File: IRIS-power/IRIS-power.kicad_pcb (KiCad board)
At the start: 2 copper layers, 65 x 65 mm, 84 parts, among them J11 Powerpole, J12 PJ-047AH, J13 Conn_01x20_MountingPin, Q21 2N7002, Q61 DMP2066LSN-7, U21 MAX17261, U31 TPS2121, U41 TPS55340, U51 TPSM53604, U61 LTC3110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

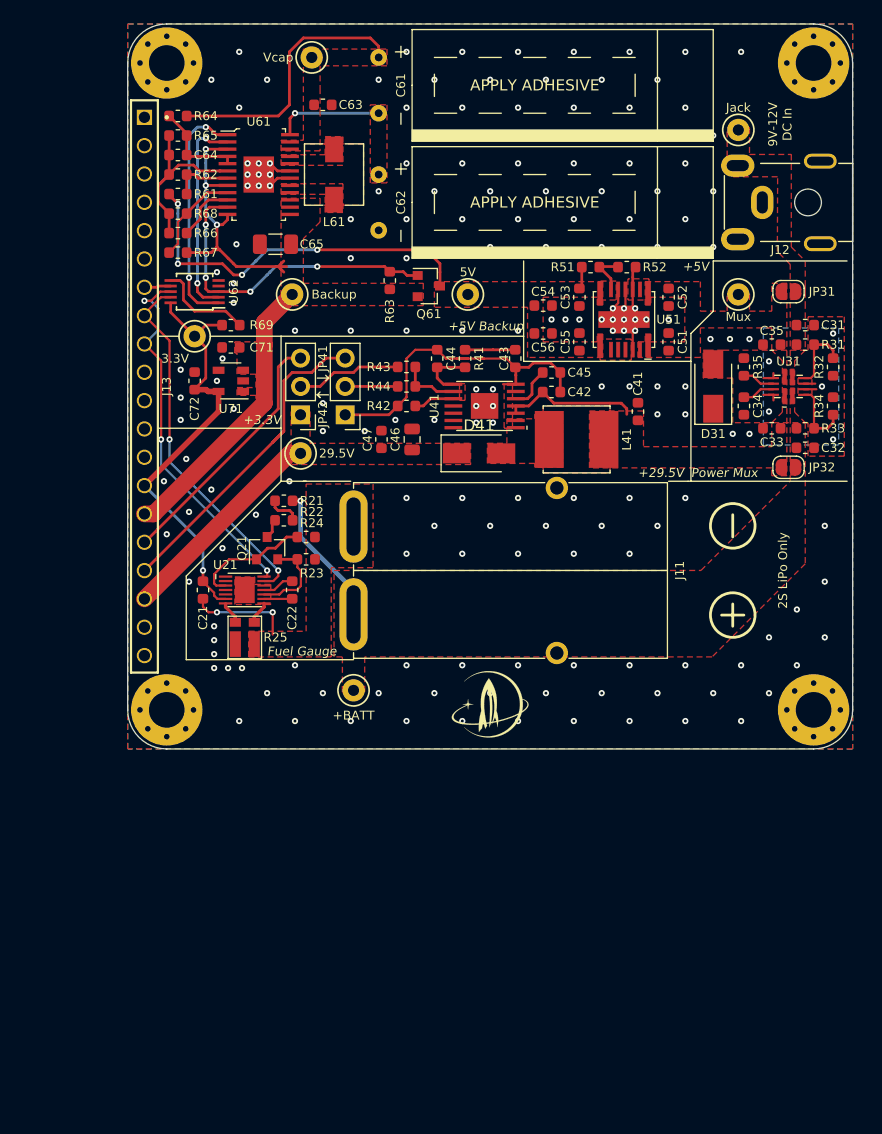
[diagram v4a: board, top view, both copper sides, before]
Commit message: USB C power prototype
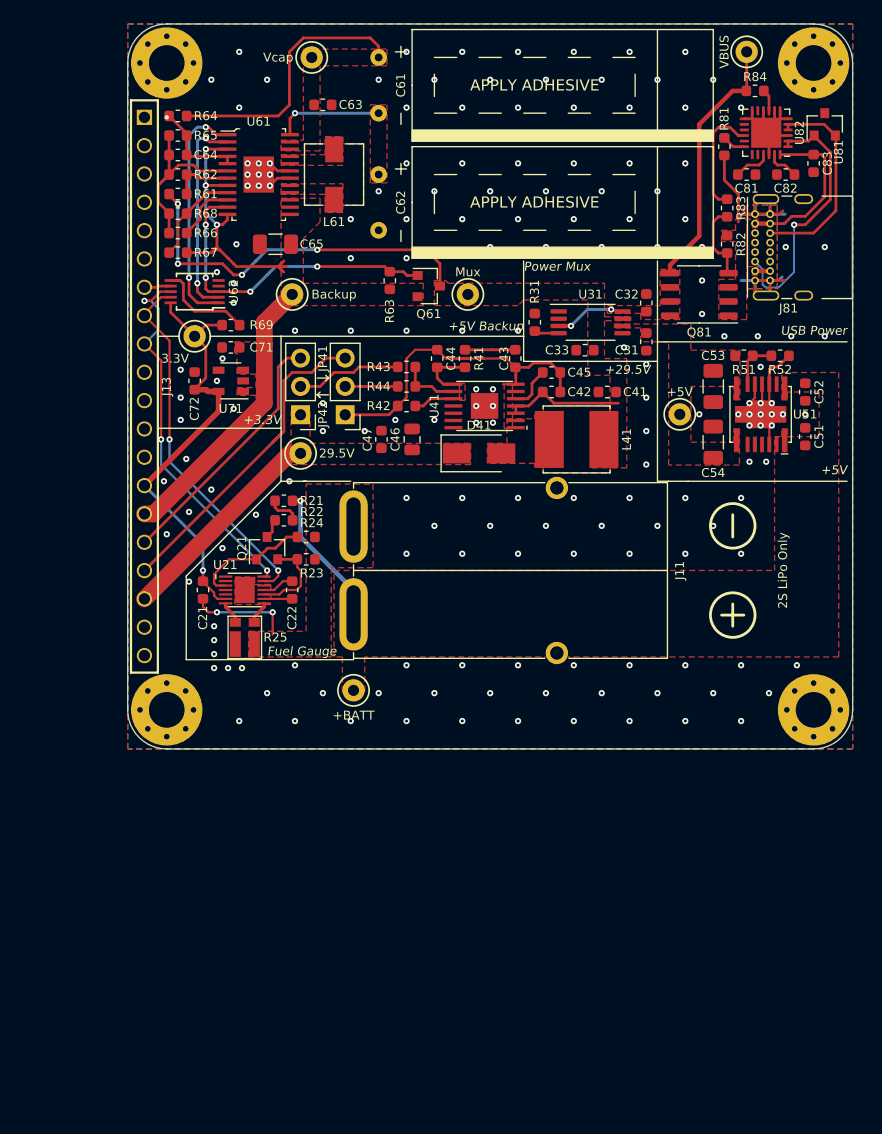
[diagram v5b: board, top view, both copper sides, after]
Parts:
- removed C34: 1uF, Capacitor_SMD:C_0603_1608Metric
- removed C35, C55, C56: 10uF, Capacitor_SMD:C_0603_1608Metric
- removed D31: D_Schottky, Diode_SMD:D_SMA
- removed G***: LOGO, star-common-lib:star_7x6
- removed J12: PJ-047AH, star-common-lib:CUI_PJ-047AH
- removed JP31: DC Jack Bypass, Jumper:SolderJumper-2_P1.3mm_Open_RoundedPad1.0x1.5mm
- removed JP32: Battery Bypass, Jumper:SolderJumper-2_P1.3mm_Open_RoundedPad1.0x1.5mm
- removed R32: 1k, Resistor_SMD:R_0603_1608Metric
- removed R33: 10k, Resistor_SMD:R_0603_1608Metric
- removed R34: 2.49k, Resistor_SMD:R_0603_1608Metric
- removed R35: 38.3k, Resistor_SMD:R_0603_1608Metric
- added C81: 1uF, Capacitor_SMD:C_0603_1608Metric, F.Cu at (55.5, -19.0)
- added C82: 1uF, Capacitor_SMD:C_0603_1608Metric, F.Cu at (59.0, -19.0)
- added C83: 1uF, Capacitor_SMD:C_0603_1608Metric, F.Cu at (61.5, -20.0)
- added J81: USB_C_Receptacle_USB2.0, Connector_USB:USB_C_Receptacle_GCT_USB4085, F.Cu at (56.2, -9.50)
- added Q81: STS9P3LLH6, Package_SO:SOP-8_3.9x4.9mm_P1.27mm, F.Cu at (51.2, -8.25)
- added R81: 1k, Resistor_SMD:R_0603_1608Metric, F.Cu at (53.5, -21.5)
- added R82: 100k, Resistor_SMD:R_0603_1608Metric, F.Cu at (53.8, -12.8)
- added R83: 20k, Resistor_SMD:R_0603_1608Metric, F.Cu at (53.8, -16.0)
- added R84: 1k, Resistor_SMD:R_0603_1608Metric, F.Cu at (56.2, -26.5)
- added U81: TPD2E2U06, Package_TO_SOT_SMD:SOT-23, F.Cu at (62.5, -23.5)
- added U82: STUSB4500LQTR, Package_DFN_QFN:QFN-24-1EP_4x4mm_P0.5mm_EP2.7x2.7mm, F.Cu at (57.2, -22.8)
- C31, C32: value 10uF -> 0.1uF
- C53, C54: value 10uF -> 47uF; footprint Capacitor_SMD:C_0603_1608Metric -> Capacitor_SMD:C_1206_3216Metric
- R31: value 2.49k -> 400R
- R66: value 3k -> 10k
- TP101: value Jack -> VBUS
- TP102: value Mux -> +5V
- TP104: value 5V -> Mux
- U31: value TPS2121 -> TPS2115APW; footprint star-common-lib:TPS2121 -> Package_SO:TSSOP-8_4.4x3mm_P0.65mm
- moved R31 24.3 mm to (36.5, -5.75), turned to 90 degrees
- moved C54 19.6 mm to (52.5, 5.00), turned to 90 degrees
- moved C32 19.3 mm to (46.5, -7.50), turned to 90 degrees
- moved U31 18.7 mm to (41.5, -5.75), turned to 0 degrees
- moved C33 18.2 mm to (41.0, -3.25)
- moved R51 15.9 mm to (55.2, -2.75)
- moved R52 15.9 mm to (58.5, -2.75)
- moved C51 14.9 mm to (60.8, 4.50)
- moved C52 14.9 mm to (60.8, 0.50)
- moved NT51 14.9 mm to (57.5, -0.94)
- moved U51 14.9 mm to (56.8, 2.50)
- moved C53 14.4 mm to (52.5, 0.00)
- moved C31 14.3 mm to (46.5, -4.00), turned to 270 degrees
- moved TP102 12.0 mm to (49.5, 2.50)
- moved TP101 7.04 mm to (55.5, -30.0)
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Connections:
- C31 pad 1: /Power Mux/VDC -> /5V Supply/+5V
- C31 pad 2: /Power Mux/GND_P -> GND
- C32 pad 1: /Fuel Gauge/+BATT -> /Power Mux/VUSB
- C32 pad 2: /Power Mux/GND_P -> GND
- C33 pad 1: /5V Supply/+MUX -> /5V Backup/+MUX
- C41 pad 1: /5V Supply/+MUX -> /5V Backup/+MUX
- C42 pad 1: /5V Supply/+MUX -> /5V Backup/+MUX
- C51 pad 1: /5V Supply/+MUX -> /5V Supply/+BATT
- C52 pad 1: /5V Supply/+MUX -> /5V Supply/+BATT
- C53 pad 1: /5V Backup/+5V -> /5V Supply/+5V
- C54 pad 1: /5V Backup/+5V -> /5V Supply/+5V
- J11 pad 1: /Fuel Gauge/+BATT -> /5V Supply/+BATT
- L41 pad 1: /5V Supply/+MUX -> /5V Backup/+MUX
- Q61 pad 3: /5V Backup/+5V -> /5V Backup/+MUX
- R21 pad 1: /Fuel Gauge/+BATT -> /5V Supply/+BATT
- R31 pad 1: /Power Mux/VDC -> Net-(R31-Pad1)
- R31 pad 2: /Power Mux/PRI -> GND
- R51 pad 1: /5V Backup/+5V -> /5V Supply/+5V
- R61 pad 1: /5V Backup/+5V -> /5V Backup/+MUX
- TP101 pad 1: /Power Mux/VDC -> /Power Mux/VUSB
- TP102 pad 1: /5V Supply/+MUX -> /5V Supply/+5V
- TP103 pad 1: /Fuel Gauge/+BATT -> /5V Supply/+BATT
- TP104 pad 1: /5V Backup/+5V -> /5V Backup/+MUX
- U31 pad 1: /5V Supply/+MUX -> Net-(U31-Pad1)
- U31 pad 2: /Fuel Gauge/+BATT -> GND
- U31 pad 3: /Power Mux/CP2 -> /Power Mux/VUSB
- U31 pad 4: /Power Mux/GND_P -> Net-(R31-Pad1)
- U31 pad 5: /Power Mux/GND_P -> GND
- U31 pad 6: /Power Mux/PRI -> /5V Supply/+5V
- U31 pad 7: /Power Mux/VDC -> /5V Backup/+MUX
- U31 pad 8: /5V Supply/+MUX -> /Power Mux/VUSB
- U41 pad 3: /5V Supply/+MUX -> /5V Backup/+MUX
- U41 pad 4: /5V Supply/+MUX -> /5V Backup/+MUX
- U51 pad 1: /5V Supply/+MUX -> /5V Supply/+BATT
- U51 pad 14: /5V Supply/+MUX -> /5V Supply/+BATT
- U51 pad 2: /5V Supply/+MUX -> /5V Supply/+BATT
- U51 pad 7: /5V Backup/+5V -> /5V Supply/+5V
- U51 pad 8: /5V Backup/+5V -> /5V Supply/+5V
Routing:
- net /5V Backup/+MUX: track 0.00 -> 44.7 mm, vias 0 -> 4
- net GND: track 12.5 -> 53.6 mm, vias 182 -> 183
- net /5V Backup/+5V: track 35.9 -> 0.00 mm, vias 4 -> 0
- net /Power Mux/VUSB: track 0.00 -> 29.7 mm, vias 0 -> 2
- net /USB Connector/CC1: track 0.00 -> 23.7 mm, vias 0 -> 1
- net /USB Connector/VBUS: track 0.00 -> 22.9 mm
- net /USB Connector/CC2: track 0.00 -> 18.7 mm
- net /Fuel Gauge/+BATT: track 12.9 -> 0.00 mm, vias 1 -> 0
- net /5V Supply/+BATT: track 0.00 -> 12.9 mm, vias 0 -> 1
- net /5V Supply/+MUX: track 12.2 -> 0.00 mm
- net Net-(R83-Pad2): track 0.00 -> 10.3 mm
- net Net-(Q81-Pad4): track 0.00 -> 7.28 mm
- net /Power Mux/PRI: track 6.40 -> 0.00 mm
- net /Power Mux/CP2: track 6.40 -> 0.00 mm
- net /Power Mux/GND_P: track 4.95 -> 0.00 mm, vias 5 -> 0
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- added copper zone on F.Cu, net /5V Backup/+MUX
- added copper zone on F.Cu, net /5V Supply/+5V
- added copper zone on F.Cu, net /5V Supply/+BATT
- added copper zone on F.Cu, net /Power Mux/VUSB
- added copper zone on F.Cu, net /USB Connector/VBUS
- removed copper zone on F.Cu, net /5V Backup/+5V
- removed copper zone on F.Cu, net /5V Supply/+MUX
- removed copper zone on F.Cu, net /Fuel Gauge/+BATT
- removed copper zone on B.Cu, net /Power Mux/GND_P
- removed copper zone on F.Cu, net /Power Mux/GND_P
- removed copper zone on F.Cu, net /Power Mux/VDC
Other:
- net class Ulow Clearance added: clearance 0.16, trace_width 0.16, via_dia 0.5588, via_drill 0.254
- board text added: "USB Power"
- board text removed: "9V-12V DC In"

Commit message: Updated HV supply
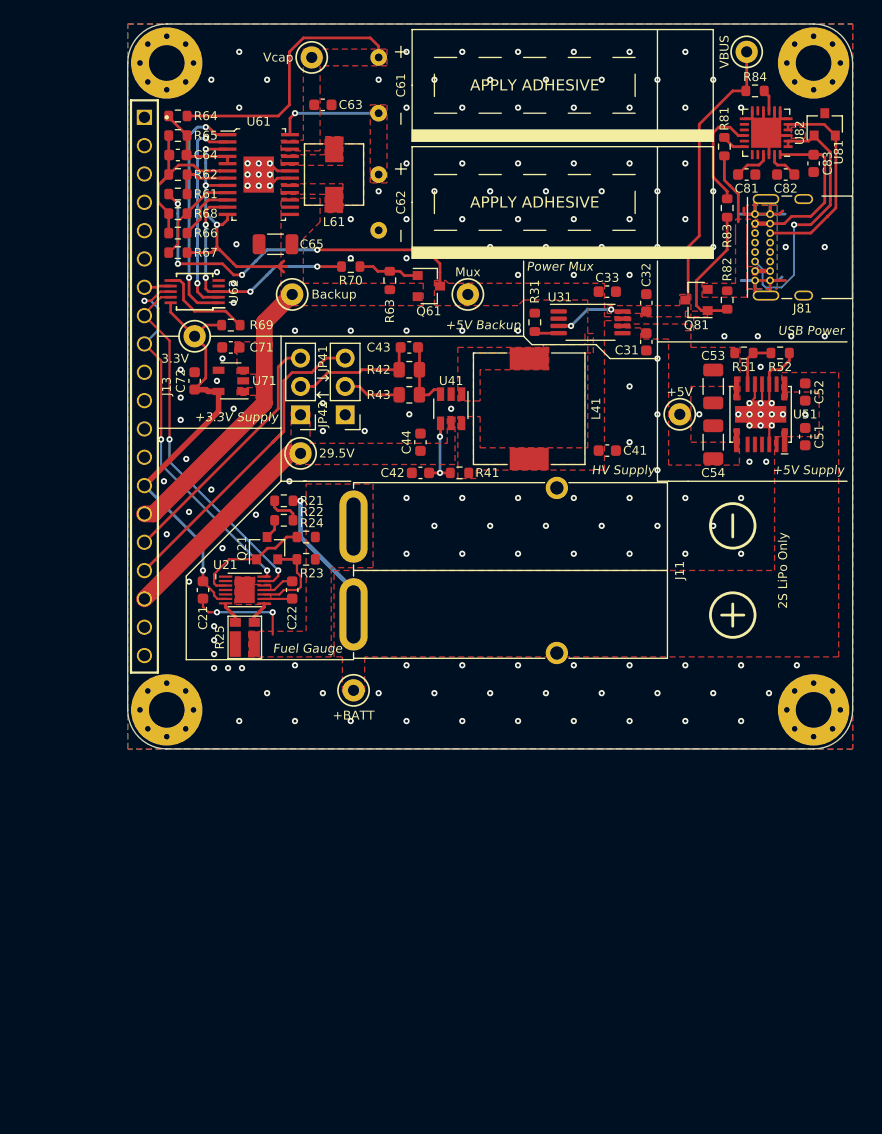
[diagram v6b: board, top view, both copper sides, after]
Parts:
- removed C45: 27nF, Capacitor_SMD:C_0603_1608Metric
- removed C46: 10uF, Capacitor_SMD:C_0805_2012Metric
- removed C47: 0.47uF, Capacitor_SMD:C_0603_1608Metric
- removed D41: D_Schottky, Diode_SMD:D_SMA
- removed NT41: Net-Tie_2, NetTie:NetTie-2_SMD_Pad0.5mm
- removed R44: 10k, Resistor_SMD:R_0603_1608Metric
- added R70: 1k, Resistor_SMD:R_0603_1608Metric, F.Cu at (20.0, -10.8)
- C41: value 10uF -> 1uF
- C42: value 0.1uF -> 47nF
- C43: value 68nF -> 22pF
- C44: value 1.2nF -> 1uF
- L41: value 8.2uH -> 22uH; footprint star-common-lib:VLS6045AF -> star-common-lib:7447714220
- Q61: value DMP2066LSN-7 -> SSM3J328R
- Q81: value STS9P3LLH6 -> SSM3J328R; footprint Package_SO:SOP-8_3.9x4.9mm_P1.27mm -> Package_TO_SOT_SMD:SOT-23
- R41: value 2.49k -> 47k
- R42: value 38.3k -> 392k; footprint Resistor_SMD:R_0603_1608Metric -> Resistor_SMD:R_0805_2012Metric
- R43: value 232k -> 17.4k; footprint Resistor_SMD:R_0603_1608Metric -> Resistor_SMD:R_0805_2012Metric
- R63: value 10k -> 100k
- R83: value 20k -> 1k
- U41: value TPS55340 -> LT3461A; footprint star-common-lib:TPS55340 -> Package_TO_SOT_SMD:TSOT-23-6
- moved C42 13.8 mm to (26.2, 7.75), turned to 180 degrees
- moved R41 10.3 mm to (29.8, 7.75), turned to 180 degrees
- moved C43 9.55 mm to (25.2, -3.50), turned to 0 degrees
- moved C44 7.65 mm to (26.2, 5.00)
- moved C33 5.62 mm to (43.0, -8.50), turned to 0 degrees
- moved C41 5.25 mm to (43.0, 5.75), turned to 0 degrees
- moved L41 5.06 mm to (36.0, 2.00)
- moved R82 5.00 mm to (53.8, -7.75)
- moved R42 3.26 mm to (25.2, -1.50)
- moved U41 3.01 mm to (29.0, 2.00), turned to 270 degrees
- moved R43 2.51 mm to (25.2, 0.75), turned to 180 degrees
- moved Q81 0.56 mm to (51.0, -7.75)
- moved R51 0.25 mm to (55.2, -3.00)
- moved R52 0.25 mm to (58.5, -3.00)
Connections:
- C42 pad 1: /5V Backup/+MUX -> Net-(C42-Pad1)
- C42 pad 2: /HV Supply/AGND -> GND
- C43 pad 2: /HV Supply/AGND -> /HV Supply/FB
- C44 pad 1: /HV Supply/COMP -> /Edge Connector/+29.5V
- C44 pad 2: /HV Supply/AGND -> GND
- JP41 pad 1: /HV Supply/AGND -> GND
- JP42 pad 2: Net-(JP42-Pad2) -> Net-(C43-Pad1)
- L41 pad 2: /HV Supply/SW -> Net-(L41-Pad2)
- Q61 pad 1: /5V Backup/~CHRG -> Net-(Q61-Pad1)
- Q81 pad 1: /USB Connector/VBUS -> Net-(Q81-Pad1)
- Q81 pad 3: /USB Connector/VBUS -> /Power Mux/VUSB
- R41 pad 1: /HV Supply/COMP -> /5V Backup/+MUX
- R41 pad 2: Net-(C43-Pad1) -> Net-(C42-Pad1)
- R42 pad 1: /HV Supply/AGND -> Net-(C43-Pad1)
- R42 pad 2: /HV Supply/FREQ -> /HV Supply/FB
- R43 pad 1: Net-(JP42-Pad2) -> /HV Supply/FB
- R43 pad 2: /HV Supply/FB -> Net-(JP41-Pad2)
- R63 pad 2: /5V Backup/~CHRG -> Net-(Q61-Pad1)
- R82 pad 2: Net-(Q81-Pad4) -> Net-(Q81-Pad1)
- R83 pad 1: Net-(Q81-Pad4) -> Net-(Q81-Pad1)
- U41 pad 1: /HV Supply/SW -> Net-(L41-Pad2)
- U41 pad 2: /HV Supply/SW -> GND
- U41 pad 3: /5V Backup/+MUX -> /HV Supply/FB
- U41 pad 4: /5V Backup/+MUX -> Net-(C42-Pad1)
- U41 pad 5: /HV Supply/SS -> /Edge Connector/+29.5V
- U41 pad 6: Net-(U41-Pad6) -> /5V Backup/+MUX
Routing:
- net /HV Supply/AGND: track 28.6 -> 0.00 mm
- net Net-(Q81-Pad1): track 0.00 -> 12.1 mm
- net /5V Backup/+MUX: track 44.7 -> 33.9 mm
- net Net-(JP42-Pad2): track 9.44 -> 0.00 mm
- net Net-(Q81-Pad4): track 7.28 -> 0.00 mm
- net /5V Backup/~CHRG: track 30.0 -> 22.8 mm
- net Net-(C43-Pad1): track 4.50 -> 11.5 mm
- net Net-(C42-Pad1): track 0.00 -> 6.36 mm, vias 0 -> 2
- net Net-(Q61-Pad1): track 0.00 -> 5.51 mm
- net /HV Supply/COMP: track 5.14 -> 0.00 mm
- net /HV Supply/SS: track 3.96 -> 0.00 mm
- net /HV Supply/FREQ: track 3.68 -> 0.00 mm
- net /Power Mux/VUSB: track 29.7 -> 31.5 mm
- net GND: track 53.6 -> 52.5 mm, vias 183 -> 179
- net /HV Supply/FB: track 5.35 -> 6.38 mm
- added copper zone on F.Cu, net Net-(L41-Pad2)
- removed copper zone on F.Cu, net /HV Supply/SW
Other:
- board text added: "+3.3V Supply"
- board text added: "+5V Supply"
- board text added: "HV Supply"
- board text removed: "+29.5V"
- board text removed: "+3.3V"
- board text removed: "+5V"

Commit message: Updated to V4.01
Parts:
- added FB81: Ferrite_Bead, Inductor_SMD:L_0603_1608Metric, F.Cu at (48.4, -7.50)
- added G***: LOGO, star-common-lib:star_8x7, F.Cu at (32.5, 28.5)
- J13: footprint star-common-lib:IRIS_Muons_physical -> star-common-lib:IRIS_V4_power
- J81: footprint Connector_USB:USB_C_Receptacle_GCT_USB4085 -> star-common-lib:USB_C_Receptacle_GCT_USB4085_Fixed
- R31: value 400R -> 402R
- U51: value TPSM53604 -> TPSM53602
- U82: footprint Package_DFN_QFN:QFN-24-1EP_4x4mm_P0.5mm_EP2.7x2.7mm -> star-common-lib:STUSB4500L
- moved U81 6.50 mm to (60.0, -17.5)
- moved C83 6.31 mm to (56.2, -16.5), turned to 180 degrees
- moved J81 6.02 mm to (62.2, -10.0)
- moved R83 3.75 mm to (53.8, -12.2)
- moved C82 2.85 mm to (56.2, -18.2)
- moved C51 2.75 mm to (58.0, 4.50)
- moved C52 2.75 mm to (58.0, 0.50)
- moved C53 2.75 mm to (49.8, 0.00)
- moved C54 2.75 mm to (49.8, 5.00)
- moved NT51 2.75 mm to (54.8, -0.94)
- moved R51 2.75 mm to (52.5, -3.00)
- moved R52 2.75 mm to (55.8, -3.00)
- moved TP102 2.75 mm to (46.8, 2.50)
- moved U51 2.75 mm to (54.0, 2.50)
- moved C31 1.41 mm to (45.5, -3.00), turned to 180 degrees
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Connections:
- J81 pad S1: GND -> Net-(J81-PadS1)
- Q81 pad 3: /Power Mux/VUSB -> Net-(FB81-Pad2)
- R84 pad 1: /Power Mux/VUSB -> Net-(FB81-Pad2)
- TP101 pad 1: /Power Mux/VUSB -> Net-(FB81-Pad2)
- U51 pad 6: Net-(U51-Pad6) -> GND
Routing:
- net Net-(FB81-Pad2): track 0.00 -> 26.6 mm
- net /Power Mux/VUSB: track 31.5 -> 8.53 mm
- net GND: track 52.5 -> 33.4 mm, vias 179 -> 187
- net /USB Connector/VBUS: track 23.2 -> 28.7 mm
- net Net-(R83-Pad2): track 9.82 -> 14.6 mm
- net /USB Connector/CC1: track 24.1 -> 20.5 mm
- net /3V Supply/VSYS: track 52.2 -> 54.3 mm
- net Net-(Q81-Pad1): track 12.1 -> 10.2 mm
- net Net-(C81-Pad1): track 3.34 -> 1.87 mm
- net /USB Connector/CC2: track 18.6 -> 17.2 mm
- net Net-(C82-Pad1): track 2.93 -> 4.01 mm
- net /5V Backup/FB: track 8.81 -> 9.87 mm
- net /5V Backup/~CMP_OUT: track 18.5 -> 19.6 mm
- net /5V Backup/DIR: track 5.55 -> 6.56 mm
- net /5V Backup/CAP_OK: track 21.3 -> 22.1 mm
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- added copper zone on F.Cu, net Net-(FB81-Pad2)
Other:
- outline, holes or cut-outs redrawn
- net class Low Clearance: clearance 0.2 -> 0.16
- rule pad_to_mask_clearance: 0.051 -> 0.0508
- board text added: "2S LiPo"
- board text added: "IRIS Power V4.01"
- board text removed: "2S LiPo Only"

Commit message: IRIS V4.02
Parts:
- added 1.5A: TestPoint_Probe, TestPoint:TestPoint_Pad_D2.0mm, B.Cu at (53.5, -25.5)
- added 3A: TestPoint_Probe, TestPoint:TestPoint_Pad_D2.0mm, B.Cu at (53.5, -22.0)
- added FID1: Fiducial, Fiducial:Fiducial_1.5mm_Mask3mm, F.Cu at (9.00, -29.0)
- added FID2: Fiducial, Fiducial:Fiducial_1.5mm_Mask3mm, F.Cu at (9.00, 29.0)
- added FID3: Fiducial, Fiducial:Fiducial_1.5mm_Mask3mm, F.Cu at (56.0, 29.0)
- added R32: 10k, Resistor_SMD:R_0603_1608Metric, F.Cu at (43.0, -10.2)
- U51: footprint star-common-lib:TPSM53604 -> star-common-lib:TPSM53602
- moved C53 10.1 mm to (58.5, 5.00), turned to 90 degrees
- moved C54 10.1 mm to (58.5, 0.00), turned to 270 degrees
- moved C51 8.94 mm to (50.0, 0.50), turned to 270 degrees
- moved C52 8.94 mm to (50.0, 4.50), turned to 90 degrees
- moved TP102 6.26 mm to (48.1, -3.60)
- moved R52 3.58 mm to (52.2, -2.25), turned to 180 degrees
- moved R51 3.34 mm to (55.8, -2.25), turned to 180 degrees
- moved TP104 2.00 mm to (32.5, -8.25)
- moved NT51 1.31 mm to (53.5, -0.84)
- moved C31 0.27 mm to (45.2, -3.10)
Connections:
- U21 pad 1: Net-(U21-Pad1) -> /3V Supply/+3.3V
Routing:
- net GND: track 33.4 -> 48.6 mm, vias 187 -> 188
- net /Power Mux/VUSB: track 8.53 -> 13.3 mm
- net Net-(TP81-Pad1): track 0.00 -> 4.13 mm, vias 0 -> 1
- net /3V Supply/VSYS: track 54.3 -> 51.1 mm, vias 3 -> 4
- net /3V Supply/+3.3V: track 39.8 -> 42.4 mm, vias 1 -> 2
- net Net-(TP82-Pad1): track 0.00 -> 2.27 mm, vias 0 -> 1
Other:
- net class Default: clearance 0.25 -> 0.16
- rule trace_clearance: 0.25 -> 0.16
- board text added: "+29.5V Supply"
- board text added: "IRIS Power V4.02"
- board text removed: "HV Supply"
- board text removed: "IRIS Power V4.01"
